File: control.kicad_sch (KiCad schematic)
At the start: 10 parts, among them IC10 INA260AIPWR, IC15 RP2354A, IC16 TPS2121RUXR, IC17 TCAN1046AVDRQ1, Q7 BSZ067N06LS3_G, Y1 ABM8-272-T3

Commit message: Test commit
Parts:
- removed D1: CUS10S30, CUS357H3F, symbol HEDGE2:CUS10S30
- removed IC15: RP2354A, QFN40P700X700X90-61N-D, symbol HEDGE2:RP2354A
- removed Q7: BSZ067N06LS3_G, BSZ067N06LS3G, symbol HEDGE2:BSZ067N06LS3_G
- removed Y1: ABM8-272-T3, ABM8272T3, symbol HEDGE2:ABM8-272-T3
- added C58, C59, C60, C61, C62, C63, C64, C66, C67, C75: 100n, symbol Device:C_Small
- added C65, C70, C71, C72: 4u7, symbol Device:C_Small
- added C68, C69: 15p, symbol Device:C_Small
- added C73, C74: 1u, symbol Device:C_Small
- added D14: CDBA240LL-HF, 40V 2A, DIOM5225X250N, symbol HEDGE2:CDBA240LL-HF
- added IC15, IC21: SN65HVD1782QDRQ1, SOIC127P600X175-8N, symbol HEDGE2:SN65HVD1782QDRQ1
- added R40, R42, R51, R52: 27, symbol Device:R_Small
- added R44: 1k, symbol Device:R_Small
- added R45: 33, symbol Device:R_Small
- added R46, R48: 23k7, symbol Device:R_Small
- added R47, R49: 5k, symbol Device:R_Small
- added R50: 51k1, symbol Device:R_Small
- added R53: 10k, symbol Device:R_Small
- added U1: RP2354A_60QFN, RP2354A_60QFN_minimal:RP2350-QFN-60-1EP_7x7_P0.4mm_EP3.4x3.4mm_ThermalVias, symbol MCU_RaspberryPi_RP2350:RP2350_60QFN
- added Y2: ABM8-272-T3, Crystal:Crystal_SMD_3225-4Pin_3.2x2.5mm, symbol Device:Crystal_GND24
- L1: value AOTA-B201610S3R3-101-T -> 3u3 AOTA-B201610S3R3-101-T
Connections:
- net +EPS_IN is gone; now on net +EPS_5V: IC10.1 (IN+_1), IC10.2 (IN+_2), IC10.3 (IN+_3)
- net GND: now also IC16.3 (CP2), IC16.6 (PR1), IC16.9 (ST), IC17.2 (GND1), IC17.5 (GND2), PS1.2 (GND), C58.2, C59.2, C60.2, C61.2, C62.2, C63.2, C64.2, C65.2, C66.2, C67.2, C68.1, C69.1, C70.2, C71.2, C72.2, C73.2, C74.2, C75.2, D14.1 (K), IC15.5 (GND), IC21.5 (GND), R47.2, R49.2, R50.2, U1.1 (IOVDD), U1.11 (IOVDD), U1.20 (IOVDD), U1.30 (IOVDD), U1.38 (IOVDD), U1.39 (DVDD), U1.44 (ADC_AVDD), U1.45 (IOVDD), U1.47 (VREG_PGND), U1.53 (USB_OTP_VDD), U1.54 (QSPI_IOVDD), U1.61 (GND), Y2.2, Y2.4
- net 1V1: now reaches L1.1
- net 1V1: now also C65.1, C66.1, C67.1, C71.1, U1.50 (VREG_FB)
- net at L1.2: now also U1.48 (VREG_LX)
- net +EPS_5V: now reaches IC16.1 (OUT_1)
- net +EPS_5V: now also IC10.12 (VBUS), IC16.8 (OUT_2)
- net at IC16.10 (ILIM): now also R50.1
- net at IC16.11 (SS): now also C75.1
- net at IC16.12 (GND): now also D14.2 (A)
- net +5V_BUCK_BOOST: now reaches IC16.2 (IN2)
- net +5V_BUCK_BOOST: now also R48.1
- net at IC16.4 (OV2): now also R48.2, R49.1
- net OV1: now reaches IC16.5 (OV1)
- net OV1: now also R46.2, R47.1
- net USB_5V: now reaches IC16.7 (IN1)
- net USB_5V: now also R46.1
- net -EPS_5V: now reaches PS1.1 (IN)
- net -EPS_5V: now also IC10.14 (IN-_1), IC10.15 (IN-_2), IC10.16 (IN-_3), IC17.3 (VCC), C73.1
- net 3V3: now reaches PS1.5 (OUT)
- net 3V3: now also IC17.11 (VIO), C58.1, C59.1, C60.1, C61.1, C62.1, C63.1, C64.1, C72.1, C74.1, IC15.8 (VCC), IC21.8 (VCC), R45.1, R53.1, U1.49 (VREG_VIN)
- net TX1: now reaches IC17.1 (TXD1)
- net CANL1: now reaches IC17.12 (CANL1)
- net CANH1: now reaches IC17.13 (CANH1)
- net STB1: now reaches IC17.14 (STB1_/_NSTB1)
- net RX1: now reaches IC17.4 (RXD1)
- removed net -EPS_IN: IC10.12 (VBUS), IC10.14 (IN-_1), IC10.15 (IN-_2), IC10.16 (IN-_3)
- new net: C68.2, U1.21 (XIN), Y2.1
- new net: C69.2, R44.1, Y2.3
- new net: R53.2, U1.26 (RUN)
- new net: R44.2, U1.22 (XOUT)
- new net: C70.1, R45.2, U1.46 (VREG_AVDD)
- new net: R42.1, U1.51 (USB_DM)
- new net: R40.1, U1.52 (USB_DP)
- new net PAY1_A: IC15.6 (A)
- new net PAY1_B: IC15.7 (B)
- new net PAY1_DE: IC15.3 (DE)
- new net PAY1_DI: IC15.4 (D)
- new net PAY1_RE: IC15.2 (RE)
- new net PAY1_RO: IC15.1 (R)
- new net PAY2_A: IC21.6 (A)
- new net PAY2_B: IC21.7 (B)
- new net PAY2_DE: IC21.3 (DE)
- new net PAY2_DI: IC21.4 (D)
- new net PAY2_RE: IC21.2 (RE)
- new net PAY2_RO: IC21.1 (R)
- new net SWCLK: U1.24 (SWCLK)
- new net SWD: U1.25 (SWD)
- new net USB_D+: R40.2
- new net USB_D-: R42.2
- no-connect marks 2 -> 15
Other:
- moved on the sheet: C13, IC10, IC16, IC17, L1, PS1

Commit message: updated battery sheet passives values
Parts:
- removed U1: RP2354A_60QFN, RP2354A_60QFN_minimal:RP2350-QFN-60-1EP_7x7_P0.4mm_EP3.4x3.4mm_ThermalVias, symbol MCU_RaspberryPi_RP2350:RP2350_60QFN
- added U2: RP2354A_60QFN, RP2354A_60QFN_minimal:RP2350-QFN-60-1EP_7x7_P0.4mm_EP3.4x3.4mm_ThermalVias, symbol MCU_RaspberryPi_RP2350:RP2350_60QFN
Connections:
- net 1V1: now also U2.50 (VREG_FB)
- net 3V3: now also U2.49 (VREG_VIN)
- net GND: now also U2.1 (IOVDD), U2.11 (IOVDD), U2.20 (IOVDD), U2.30 (IOVDD), U2.38 (IOVDD), U2.39 (DVDD), U2.44 (ADC_AVDD), U2.45 (IOVDD), U2.47 (VREG_PGND), U2.53 (USB_OTP_VDD), U2.54 (QSPI_IOVDD), U2.61 (GND)
- net SWCLK: now also U2.24 (SWCLK)
- net SWD: now also U2.25 (SWD)
- net at C68.2, Y2.1: now also U2.21 (XIN)
- net at R53.2: now also U2.26 (RUN)
- net at R44.2: now also U2.22 (XOUT)
- net at C70.1, R45.2: now also U2.46 (VREG_AVDD)
- net at L1.2: now also U2.48 (VREG_LX)
- net at R42.1: now also U2.51 (USB_DM)
- net at R40.1: now also U2.52 (USB_DP)
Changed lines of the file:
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@@
+	)
+	(symbol
+		(lib_id "MCU_RaspberryPi_RP2350:RP2350_60QFN")
+		(at 116.84 124.46 0)
+		(unit 1)
+		(exclude_from_sim no)
+		(in_bom yes)
+		(on_board yes)
+		(dnp no)
+		(fields_autoplaced yes)
+		(property "Reference" "U2"
+			(at 118.9833 175.26 0)
+			(effects
+				(font
+					(size 1.27 1.27)
+				)
+				(justify left)
+			)
+		)
+		(property "Value" "RP2354A_60QFN"
+			(at 118.9833 177.8 0)
+			(effects
+				(font
+					(size 1.27 1.27)
+				)
+				(justify left)
+			)
+		)
+		(property "Footprint" "RP2354A_60QFN_minimal:RP2350-QFN-60-1EP_7x7_P0.4mm_EP3.4x3.4mm_ThermalVias"
+			(at 97.79 124.46 0)
+			(effects
+				(font
+					(size 1.27 1.27)
+				)
+				(hide yes)
+			)
+		)
+		(property "Datasheet" ""
+			(at 97.79 124.46 0)
+			(effects
+				(font
+					(size 1.27 1.27)
+				)
+				(hide yes)
+			)
+		)
+		(property "Description" ""
+			(at 116.84 124.46 0)
+			(effects
+				(font
+					(size 1.27 1.27)
+				)
+			)
+		)
+		(pin "24"
+		)
+		(pin "21"
+		)
+		(pin "30"
+		)
+		(pin "38"
+		)
+		(pin "1"
+		)
+		(pin "50"
+		)
+		(pin "45"
+		)
+		(pin "2"
+		)
+		(pin "22"
+		)
+		(pin "39"
+		)
+		(pin "23"
+		)
+		(pin "44"
+		)
+		(pin "26"
+		)
+		(pin "6"
+		)
+		(pin "25"
+		)
+		(pin "57"
+		)
+		(pin "47"
+		)
+		(pin "46"
+		)
+		(pin "60"
+		)
+		(pin "59"
+		)
+		(pin "58"
+		)
+		(pin "49"
+		)
+		(pin "48"
+		)
+		(pin "55"
+		)
+		(pin "56"
+		)
+		(pin "54"
+		)
+		(pin "61"
+		)
+		(pin "20"
+		)
+		(pin "11"
+		)
+		(pin "53"
+		)
+		(pin "52"
+		)
+		(pin "51"
+		)
+		(pin "16"
+		)
+		(pin "27"
+		)
+		(pin "3"
+		)
+		(pin "34"
+		)
+		(pin "32"
+		)
+		(pin "42"
+		)
+		(pin "9"
+		)
+		(pin "8"
+		)
+		(pin "18"
+		)
+		(pin "29"
+		)
+		(pin "10"
+		)
+		(pin "36"
+		)
+		(pin "14"
+		)
+		(pin "19"
+		)
+		(pin "37"
+		)
+		(pin "41"
+		)
+		(pin "13"
+		)
+		(pin "28"
+		)
+		(pin "15"
+		)
+		(pin "5"
+		)
+		(pin "4"
+		)
+		(pin "12"
+		)
+		(pin "7"
+		)
+		(pin "17"
+		)
+		(pin "33"
+		)
+		(pin "31"
+		)
+		(pin "35"
+		)
+		(pin "40"
+		)
+		(pin "43"
+		)
+		(instances
+			(project ""
+				(path "/7b605902-d0e0-4baa-b797-611cfe27637f/8396a4b2-0cce-4978-8662-437d163a7808"
+					(reference "U2")
+					(unit 1)
+				)
+			)
+		)
 	)
 	(symbol
@@
 					(unit 1)
 				)
-			)
-		)
-	)
-	(symbol
-		(lib_id "MCU_RaspberryPi_RP2350:RP2350_60QFN")
-		(at 116.84 124.46 0)
-		(unit 1)
-		(exclude_from_sim no)
-		(in_bom yes)
-		(on_board yes)
-		(dnp no)
-		(fields_autoplaced yes)
-		(property "Reference" "U1"
-			(at 119.0341 175.26 0)
-			(effects
-				(font
-					(size 1.27 1.27)
-				)
-				(justify left)
-			)
-		)
-		(property "Value" "RP2354A_60QFN"
-			(at 119.0341 177.8 0)
-			(effects
-				(font
-					(size 1.27 1.27)
-				)
-				(justify left)
-			)
-		)
-		(property "Footprint" "RP2354A_60QFN_minimal:RP2350-QFN-60-1EP_7x7_P0.4mm_EP3.4x3.4mm_ThermalVias"
-			(at 97.79 124.46 0)
-			(effects
-				(font
-					(size 1.27 1.27)
-				)
-				(hide yes)
-			)
-		)
-		(property "Datasheet" ""
-			(at 97.79 124.46 0)
-			(effects
-				(font
-					(size 1.27 1.27)
-				)
-				(hide yes)
-			)
-		)
-		(property "Description" ""
-			(at 116.84 124.46 0)
-			(effects
-				(font
-					(size 1.27 1.27)
-				)
-			)
-		)
-		(pin "1"
-		)
-		(pin "10"
-		)
-		(pin "11"
-		)
-		(pin "12"
-		)
-		(pin "13"
-		)
-		(pin "14"
-		)
-		(pin "15"
-		)
-		(pin "16"
-		)
-		(pin "17"
-		)
-		(pin "18"
-		)
-		(pin "19"
-		)
-		(pin "2"
-		)
-		(pin "20"
-		)
-		(pin "21"
-		)
-		(pin "22"
-		)
-		(pin "23"
-		)
-		(pin "24"
-		)
-		(pin "25"
-		)
-		(pin "26"
-		)
-		(pin "27"
-		)
-		(pin "28"
-		)
-		(pin "29"
-		)
-		(pin "3"
-		)
-		(pin "30"
-		)
-		(pin "31"
-		)
-		(pin "32"
-		)
-		(pin "33"
-		)
-		(pin "34"
-		)
-		(pin "35"
-		)
-		(pin "36"
-		)
-		(pin "37"
-		)
-		(pin "38"
-		)
-		(pin "39"
-		)
-		(pin "4"
-		)
-		(pin "40"
-		)
-		(pin "41"
-		)
-		(pin "42"
-		)
-		(pin "43"
-		)
-		(pin "44"
-		)
-		(pin "45"
-		)
-		(pin "46"
-		)
-		(pin "47"
-		)
-		(pin "48"
-		)
-		(pin "49"
-		)
-		(pin "5"
-		)
-		(pin "50"
-		)
-		(pin "51"
-		)
-		(pin "52"
-		)
-		(pin "53"
-		)
-		(pin "54"
-		)
-		(pin "55"
-		)
-		(pin "56"
-		)
-		(pin "57"
-		)
-		(pin "58"
-		)
-		(pin "59"
-		)
-		(pin "6"
-		)
-		(pin "60"
-		)
-		(pin "61"
-		)
-		(pin "7"
-		)
-		(pin "8"
-		)
-		(pin "9"
-		)
-		(instances
-			(project "EPS"
-				(path "/7b605902-d0e0-4baa-b797-611cfe27637f/8396a4b2-0cce-4978-8662-437d163a7808"
-					(reference "U1")
-					(unit 1)
-				)

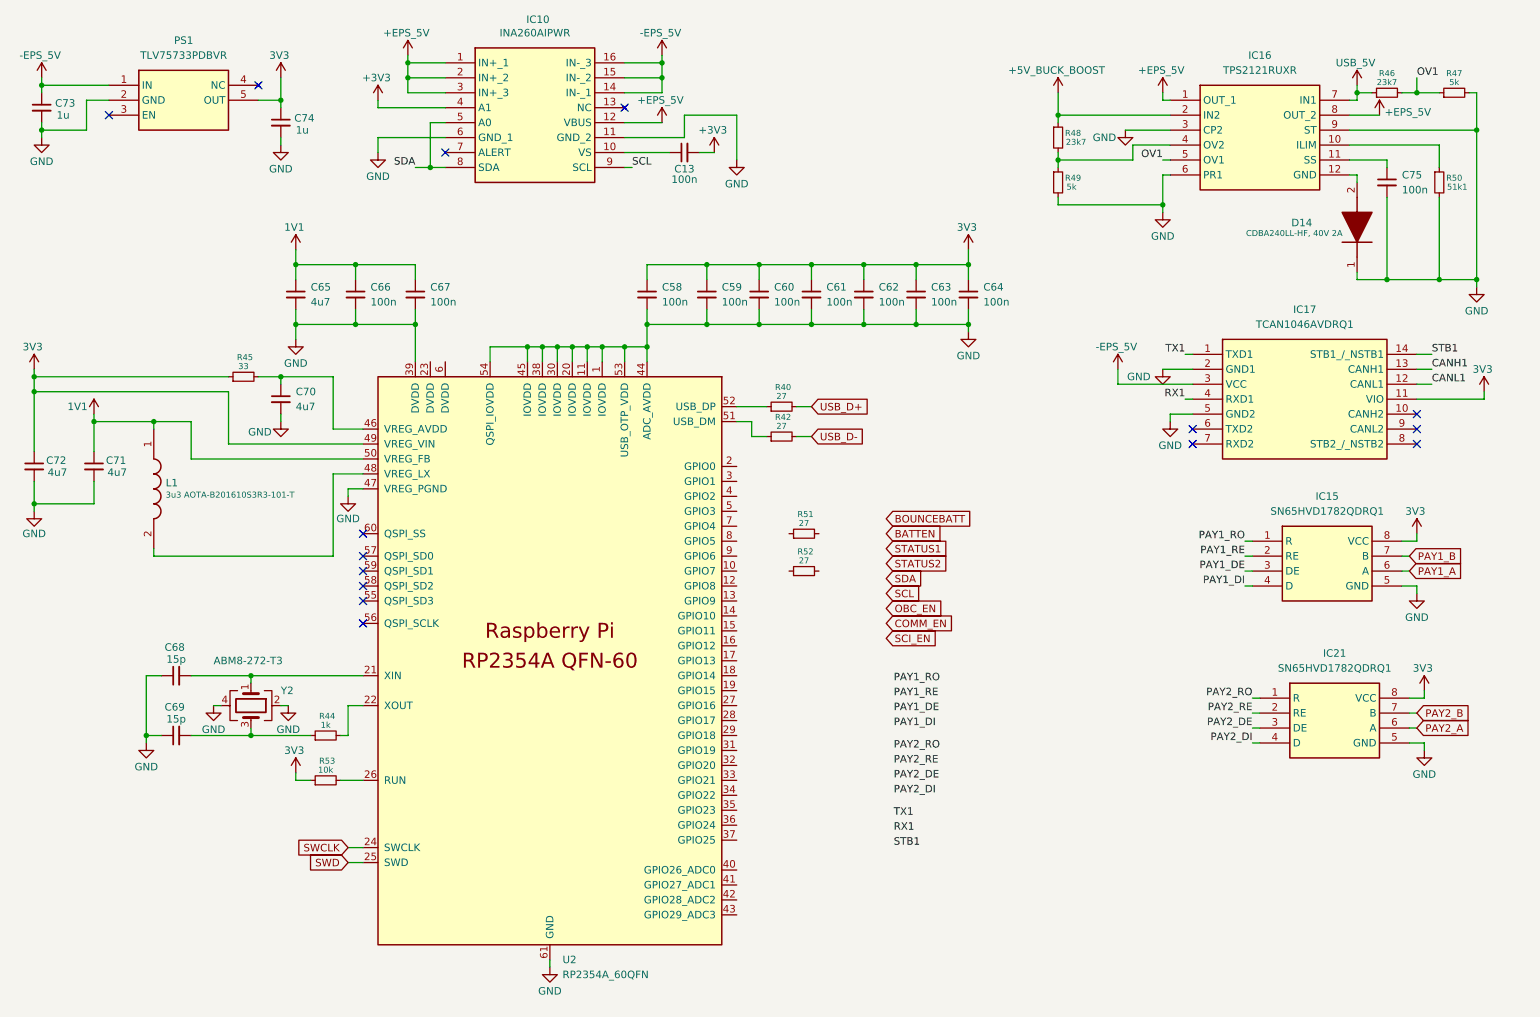
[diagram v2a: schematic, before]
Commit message: Added CAN controller, got rid of one RS485 transceiver
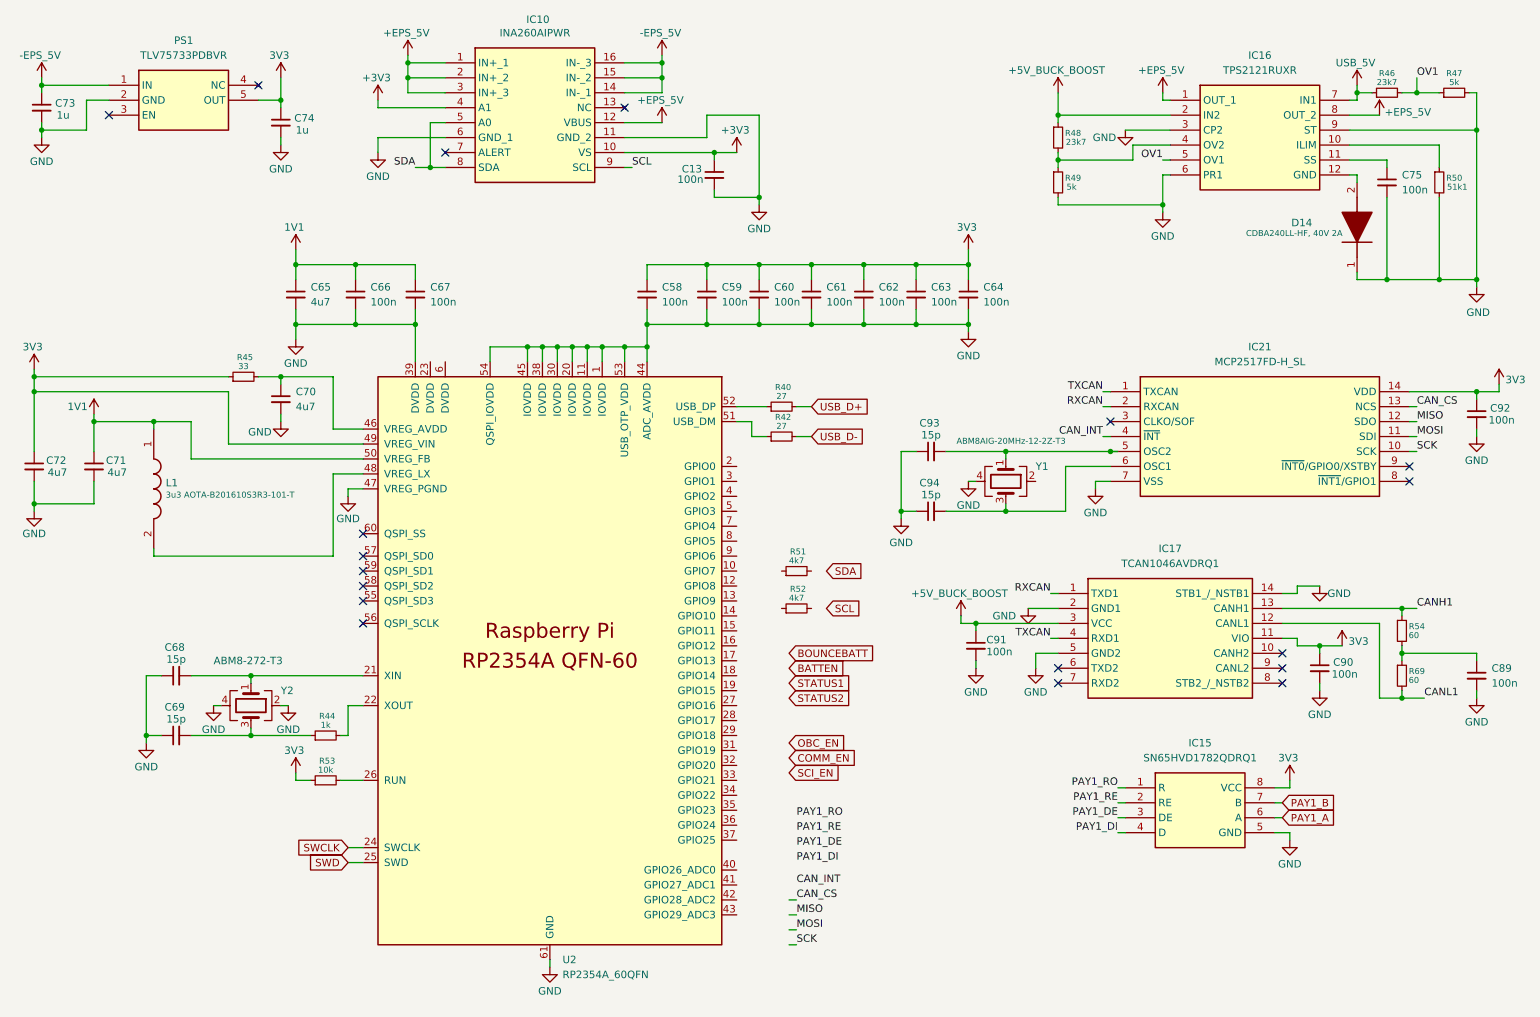
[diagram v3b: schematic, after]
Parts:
- removed IC21: SN65HVD1782QDRQ1, SOIC127P600X175-8N, symbol HEDGE2:SN65HVD1782QDRQ1
- added C89, C90, C91, C92: 100n, symbol Device:C_Small
- added C93, C94: 15p, symbol Device:C_Small
- added IC21: MCP2517FD-H_SL, SOIC127P600X175-14N, symbol HEDGE2:MCP2517FD-H_SL
- added R54, R69: 60, symbol Device:R_Small
- added Y1: ABM8AIG-20MHz-12-2Z-T3, Crystal:Crystal_SMD_3225-4Pin_3.2x2.5mm, symbol Device:Crystal_GND24
- R51, R52: value 27 -> 4k7
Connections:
- net STB1 is gone; now on net GND: IC17.14 (STB1_/_NSTB1)
- net +3V3: now also C13.1, IC10.10 (VS); no longer C13.2
- net +5V_BUCK_BOOST: now also IC17.3 (VCC), C91.1
- net -EPS_5V: no longer IC17.3 (VCC)
- net 3V3: now also C90.1, C92.1, IC21.14 (VDD)
- net CANH1: now also R54.1
- net CANL1: now also R69.2
- net GND: now also C13.2, C89.2, C90.2, C91.2, C92.2, C93.1, C94.1, IC21.7 (VSS), Y1.4
- net RX1 renamed TXCAN
- net TXCAN: now also IC21.1 (TXCAN)
- net TX1 renamed RXCAN
- net RXCAN: now also IC21.2 (RXCAN)
- new net: C89.1, R54.2, R69.1
- new net: C93.2, IC21.5 (OSC2), Y1.1
- new net: C94.2, IC21.6 (OSC1), Y1.3
- new net CAN_CS: IC21.13 (NCS)
- new net CAN_INT: IC21.4 (~{INT})
- new net MISO: IC21.12 (SDO)
- new net MOSI: IC21.11 (SDI)
- new net SCK: IC21.10 (SCK)
- no-connect marks 15 -> 18
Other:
- moved on the sheet: IC15, IC17, R51, R52

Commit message: updates to connectors
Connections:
- net PAY1_A: now also IC15.7 (B); no longer IC15.6 (A)
- net PAY1_B: now also IC15.6 (A); no longer IC15.7 (B)
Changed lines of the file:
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@@
 	(title_block
 		(title "HEDGE2 EPS")
-		(date "2025-10-12")
+		(date "2025-10-30")
 		(rev "V0.8")
 		(company "University of Virginia")
@@
 	(wire
 		(pts
-			(xy 265.43 130.81) (xy 261.62 130.81)
+			(xy 264.16 130.81) (xy 261.62 130.81)
 		)
 		(stroke
@@
 		)
 	)
-	(label "CANL1"
-		(at 265.43 130.81 0)
-		(effects
-			(font
-				(size 1.27 1.27)
-			)
-			(justify left bottom)
-		)
-	)
 	(label "PAY1_RO"
 		(at 158.75 151.13 0)
@@
 		)
 	)
-	(label "CANH1"
-		(at 264.16 115.57 0)
-		(effects
-			(font
-				(size 1.27 1.27)
-			)
-			(justify left bottom)
-		)
-	)
 	(label "PAY1_DI"
 		(at 213.36 153.67 180)
@@
 		)
 	)
-	(global_label "USB_D-"
-		(shape input)
-		(at 161.29 86.36 0)
-		(fields_autoplaced yes)
-		(effects
-			(font
-				(size 1.27 1.27)
-			)
-			(justify left)
-		)
-		(property "Intersheetrefs" "${INTERSHEET_REFS}"
-			(at 171.8952 86.36 0)
-			(effects
-				(font
-					(size 1.27 1.27)
-				)
-				(justify left)
-				(hide yes)
-			)
-		)
-	)
 	(global_label "SDA"
 		(shape input)
@@
 		)
 	)
-	(global_label "USB_D+"
-		(shape input)
-		(at 161.29 81.28 0)
-		(fields_autoplaced yes)
-		(effects
-			(font
-				(size 1.27 1.27)
-			)
-			(justify left)
-		)
-		(property "Intersheetrefs" "${INTERSHEET_REFS}"
-			(at 171.8952 81.28 0)
-			(effects
-				(font
-					(size 1.27 1.27)
-				)
-				(justify left)
-				(hide yes)
-			)
-		)
-	)
 	(global_label "STATUS2"
 		(shape input)
@@
 		)
 	)
-	(global_label "PAY1_A"
+	(hierarchical_label "CANH1"
 		(shape input)
-		(at 241.3 151.13 0)
-		(fields_autoplaced yes)
+		(at 264.16 115.57 0)
 		(effects
 			(font
@@
 			(justify left)
 		)
-		(property "Intersheetrefs" "${INTERSHEET_REFS}"
-			(at 250.9981 151.13 0)
-			(effects
-				(font
-					(size 1.27 1.27)
-				)
-				(justify left)
-				(hide yes)
+	)
+	(hierarchical_label "RBF_INHIBIT"
+		(shape input)
+		(at 157.48 181.61 0)
+		(effects
+			(font
+				(size 1.27 1.27)
+			)
+			(justify left)
+		)
+	)
+	(hierarchical_label "SWDIO"
+		(shape input)
+		(at 157.48 176.53 0)
+		(effects
+			(font
+				(size 1.27 1.27)
+			)
+			(justify left)
+		)
+	)
+	(hierarchical_label "USB_D+"
+		(shape input)
+		(at 161.29 81.28 0)
+		(effects
+			(font
+				(size 1.27 1.27)
+			)
+			(justify left)
+		)
+	)
+	(hierarchical_label "USB_D-"
+		(shape input)
+		(at 161.29 86.36 0)
+		(effects
+			(font
+				(size 1.27 1.27)
 			)
+			(justify left)
 		)
 	)
-	(global_label "PAY1_B"
+	(hierarchical_label "PAY1_B"
+		(shape input)
+		(at 241.3 151.13 0)
+		(effects
+			(font
+				(size 1.27 1.27)
+			)
+			(justify left)
+		)
+	)
+	(hierarchical_label "PAY1_A"
 		(shape input)
 		(at 241.3 148.59 0)
-		(fields_autoplaced yes)
 		(effects
 			(font
@@
 			(justify left)
 		)
-		(property "Intersheetrefs" "${INTERSHEET_REFS}"
-			(at 251.1795 148.59 0)
-			(effects
-				(font
-					(size 1.27 1.27)
-				)
-				(justify left)
-				(hide yes)
+	)
+	(hierarchical_label "CANL1"
+		(shape input)
+		(at 264.16 130.81 0)
+		(effects
+			(font
+				(size 1.27 1.27)
 			)
+			(justify left)
+		)
+	)
+	(hierarchical_label "SWCLK"
+		(shape input)
+		(at 157.48 179.07 0)
+		(effects
+			(font
+				(size 1.27 1.27)
+			)
+			(justify left)
 		)
 	)
